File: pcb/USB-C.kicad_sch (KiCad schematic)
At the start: 17 parts, among them J3 USB_C_Receptacle_USB2.0, U7 USBLC6-2SC6, U8 PMDPB70XP, U9 STUSB1600AQTR

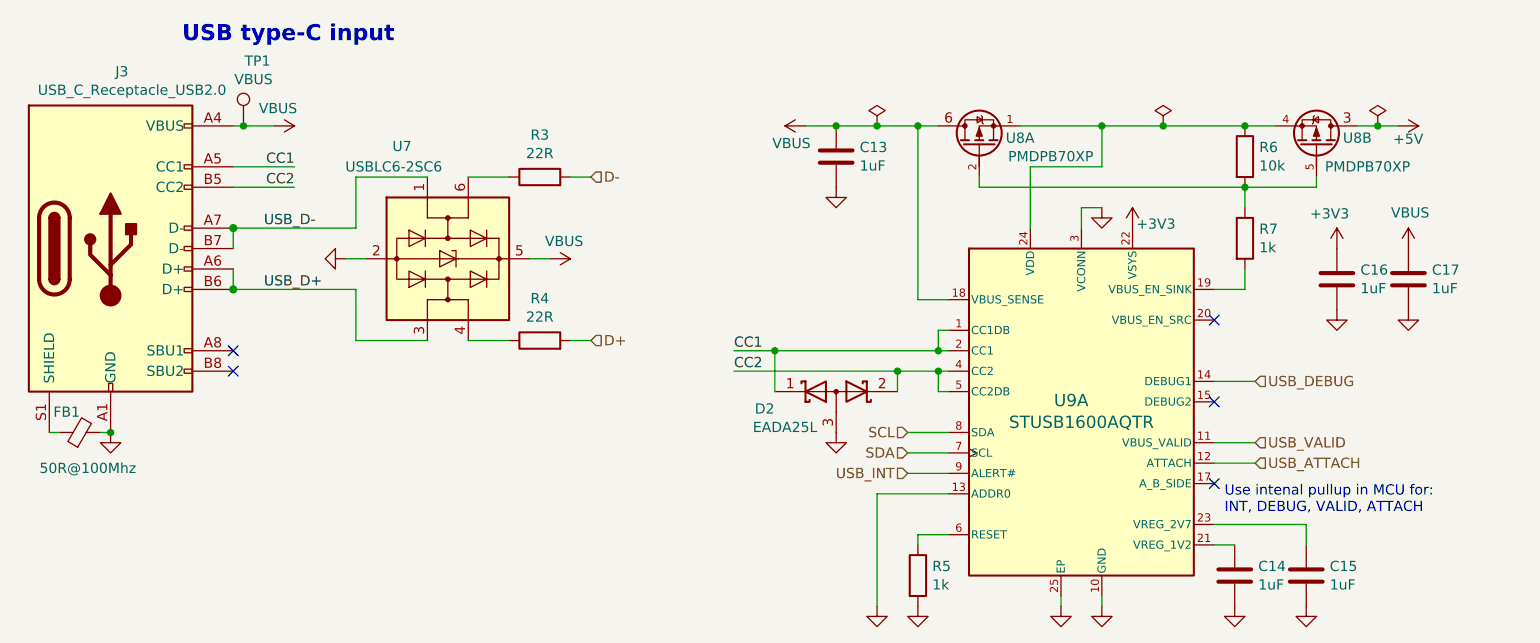
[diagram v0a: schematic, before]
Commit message: Schema & PCB: Update page layout, add notes about SPI modes and I2C addresses
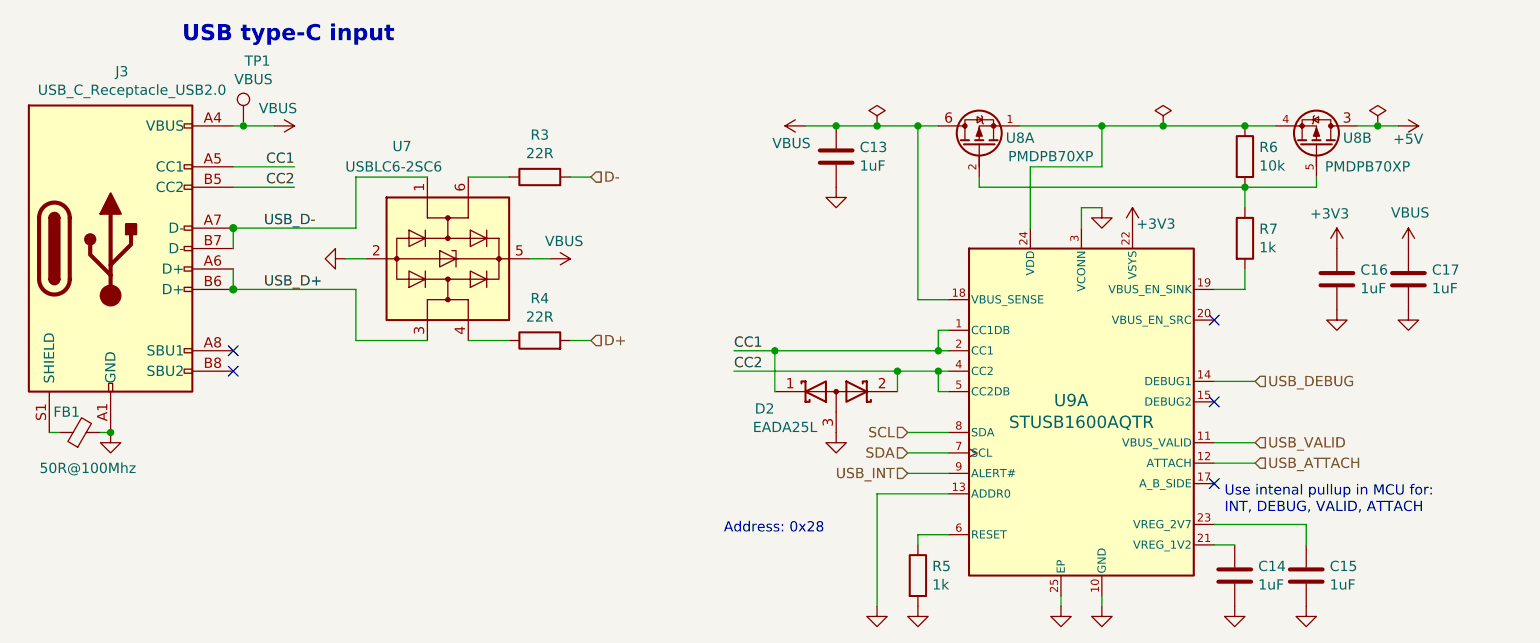
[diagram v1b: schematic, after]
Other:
- note added: "Address: 0x28"
- company: (none) -> Author: Petr Malaník
- title: (none) -> RingOne
